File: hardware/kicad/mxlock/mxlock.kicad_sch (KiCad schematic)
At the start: 26 parts, among them J1 Conn_01x02, J2 Conn_01x02, J3 Conn_01x02, J4 Conn_01x02, J5 Conn_01x04, J6 ATMEL-ICE-10, Q1 2N3904, SW1 SW_SL, SW2 SW_CAPS, SW3 SW_4080, SW4 SW_EXTRA, U1 ATtiny214/414/814, U2 CD4066BM

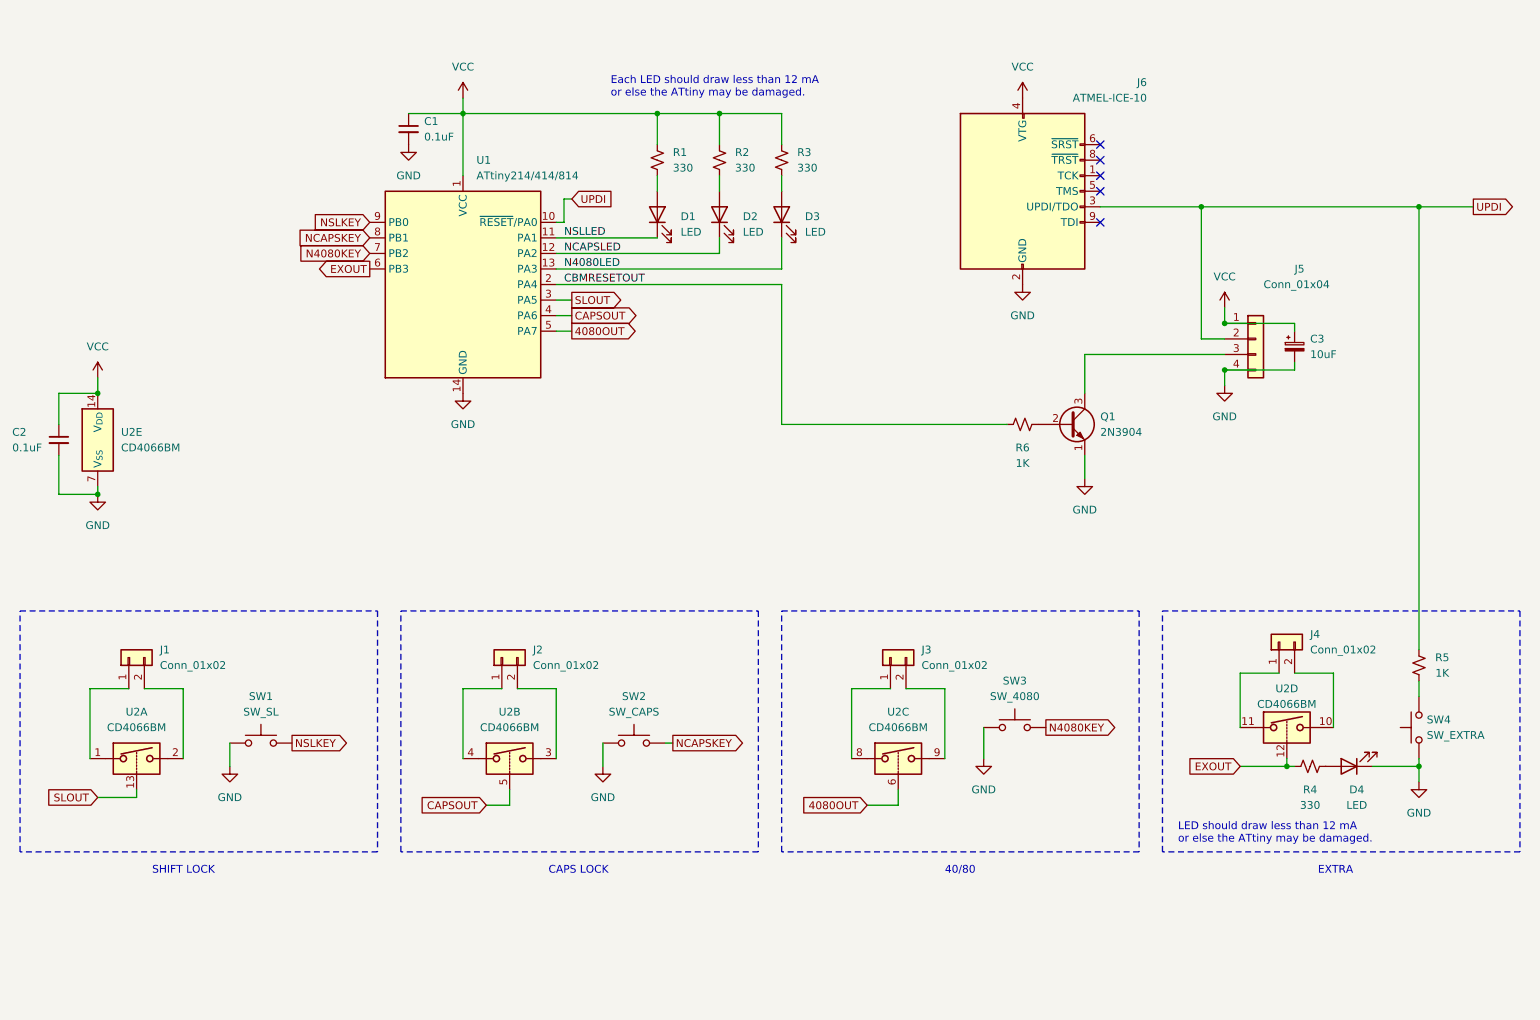
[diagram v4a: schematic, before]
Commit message: Rename keys to LOCK0-3
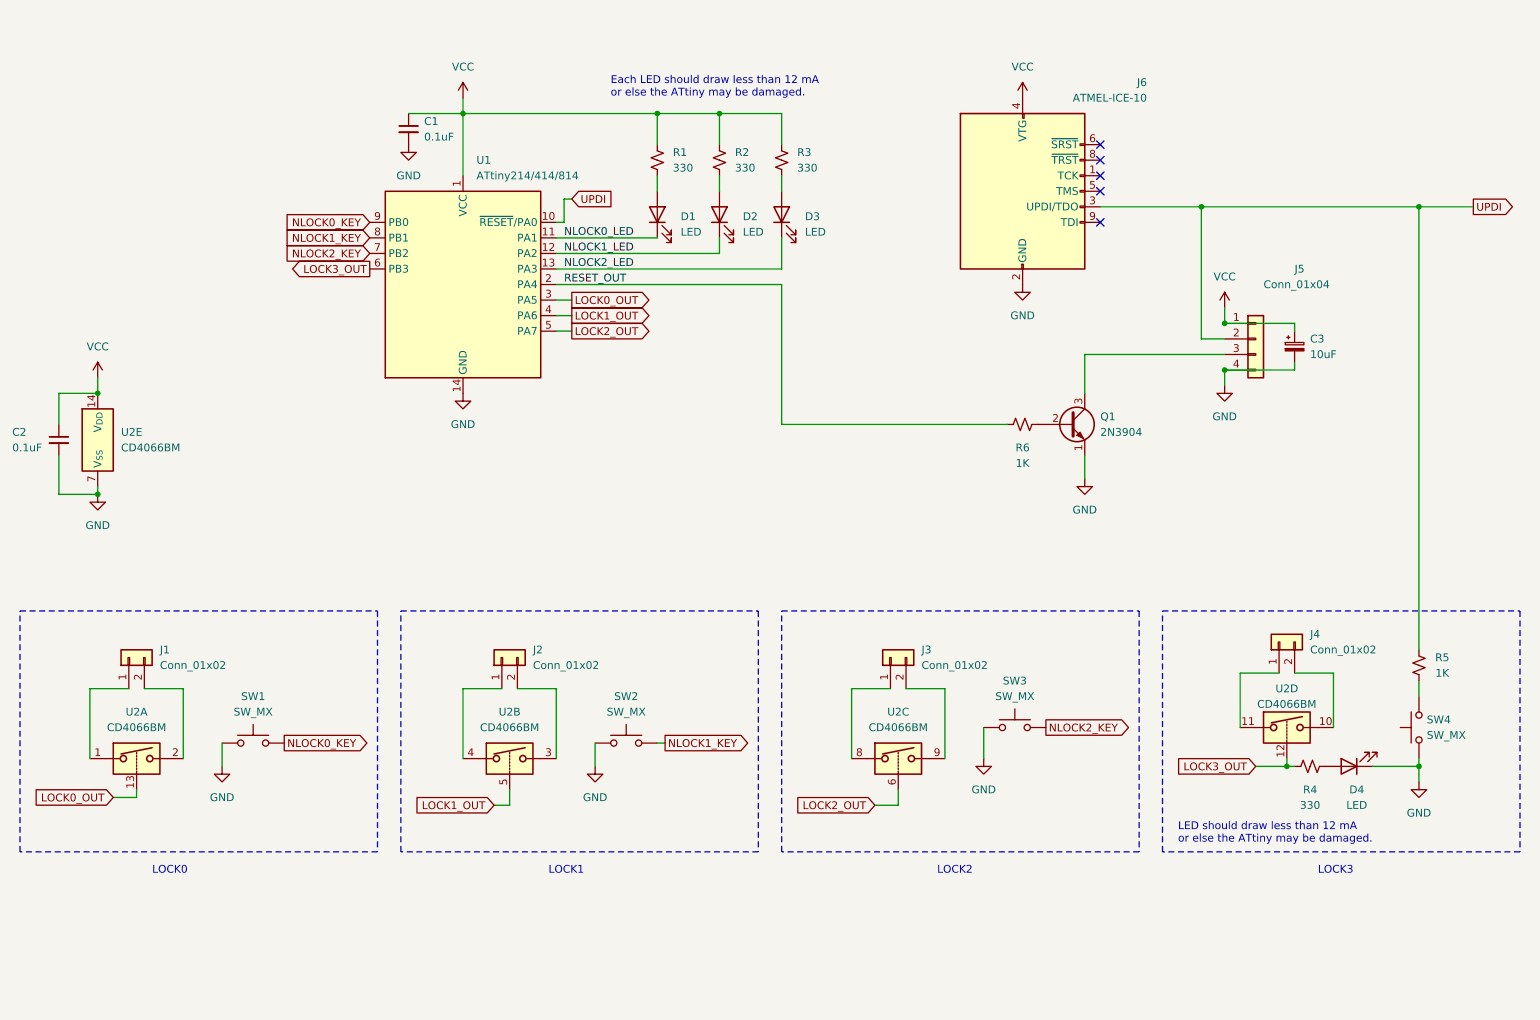
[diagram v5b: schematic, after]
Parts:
- SW1: value SW_SL -> SW_MX
- SW2: value SW_CAPS -> SW_MX
- SW3: value SW_4080 -> SW_MX
- SW4: value SW_EXTRA -> SW_MX
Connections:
- net 4080OUT renamed LOCK2_OUT
- net CAPSOUT renamed LOCK1_OUT
- net CBMRESETOUT renamed RESET_OUT
- net EXOUT renamed LOCK3_OUT
- net N4080KEY renamed NLOCK2_KEY
- net N4080LED renamed NLOCK2_LED
- net NCAPSKEY renamed NLOCK1_KEY
- net NCAPSLED renamed NLOCK1_LED
- net NSLKEY renamed NLOCK0_KEY
- net NSLLED renamed NLOCK0_LED
- net SLOUT renamed LOCK0_OUT
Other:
- note added: "LOCK0"
- note added: "LOCK1"
- note added: "LOCK2"
- note added: "LOCK3"
- note removed: "40/80"
- note removed: "CAPS LOCK"
- note removed: "EXTRA"
- note removed: "SHIFT LOCK"
- moved on the sheet: SW1, SW2

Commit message: Outline reset circuit on schematic
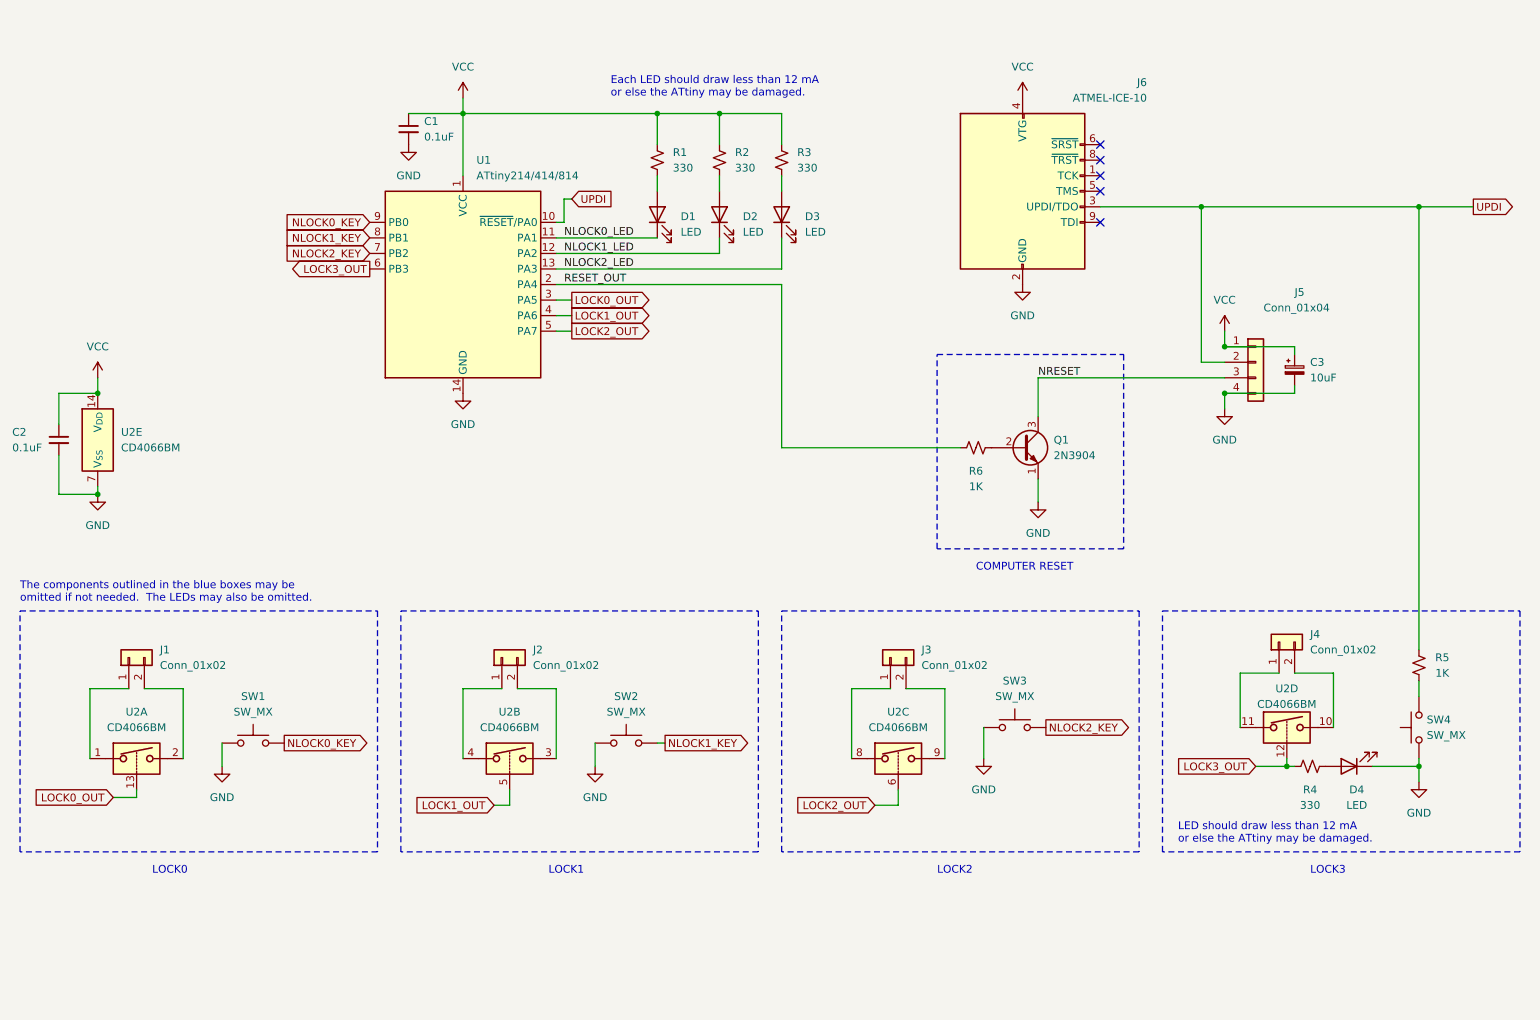
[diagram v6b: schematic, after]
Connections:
- net NRESET: now reaches J5.3 (Pin_3), Q1.3 (C)
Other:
- note added: "COMPUTER RESET"
- note added: "The components outlined in the blue boxes may be omitted if not needed. The LEDs may also be omitted."
- moved on the sheet: C3, J5, Q1, R6
